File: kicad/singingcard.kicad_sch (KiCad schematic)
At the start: 0 parts

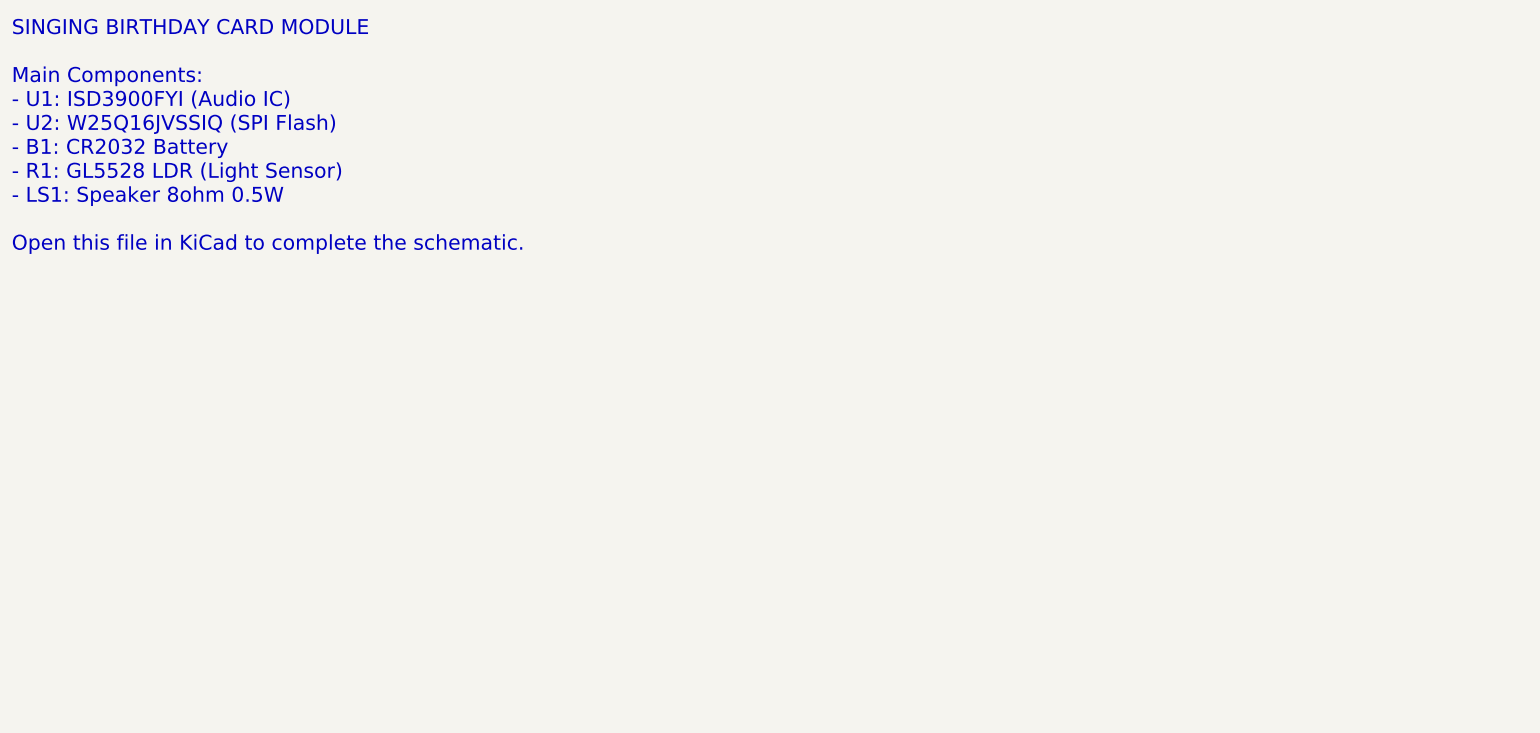
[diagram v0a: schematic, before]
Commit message: Add proper KiCad schematic with embedded symbols
- Created schematic generator scripts (v1-v5) to programmatically
  create KiCad schematics from SKiDL netlist data
- Final version (v5) places global labels at correct pin positions
- All 50 ERC violations are warnings (library config), not errors
- Updated kicad-agent.md skill with V-Model workflow approach
- Added render images for visual inspection
- Added DRC and ERC report files

🤖 Generated with [Claude Code](https://claude.com/claude-code)

Co-Authored-By: Claude <noreply@anthropic.com>
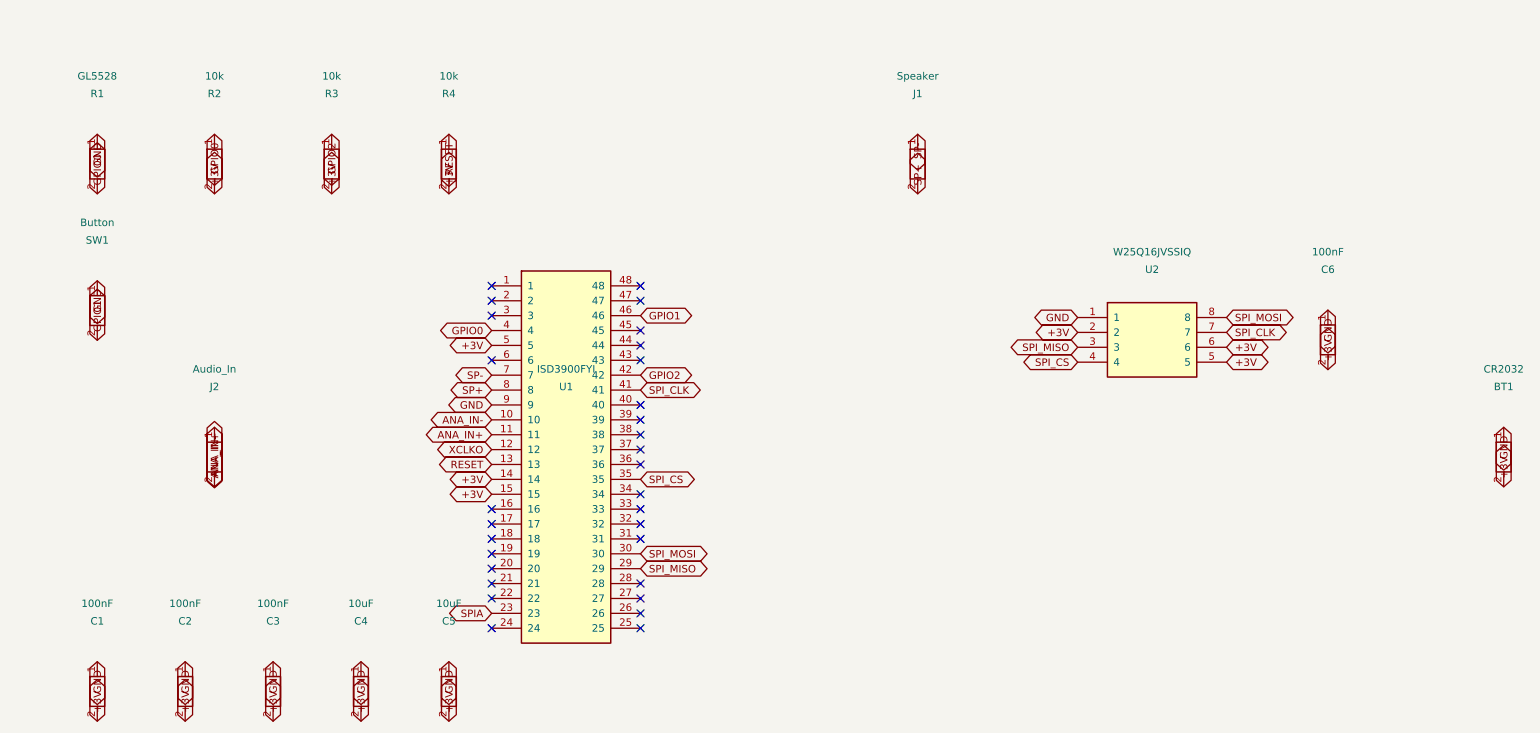
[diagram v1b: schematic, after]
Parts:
- added BT1: CR2032, singingcard:BAT-TH_CR2032-BS-6-1, symbol singingcard:CR2032
- added C1, C2, C3, C6: 100nF, Capacitor_SMD:C_0603_1608Metric, symbol singingcard:C
- added C4, C5: 10uF, Capacitor_SMD:C_0805_2012Metric, symbol singingcard:C
- added J1: Speaker, Connector_PinHeader_2.54mm:PinHeader_1x02_P2.54mm_Vertical, symbol singingcard:Conn_01x02
- added J2: Audio_In, Connector_PinHeader_2.54mm:PinHeader_1x02_P2.54mm_Vertical, symbol singingcard:Conn_01x02
- added R1: GL5528, singingcard:LDR_GL5528, symbol singingcard:LDR
- added R2, R3, R4: 10k, Resistor_SMD:R_0603_1608Metric, symbol singingcard:R
- added SW1: Button, Button_Switch_SMD:SW_SPST_B3U-1000P, symbol singingcard:SW_Push
- added U1: ISD3900FYI, singingcard:LQFP-48_7x7mm_P0.5mm, symbol singingcard:ISD3900FYI
- added U2: W25Q16JVSSIQ, singingcard:SOIC-8_5.23x5.23mm_P1.27mm, symbol singingcard:W25Q16JVSSIQ
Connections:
- new net +3V: BT1.2, C1.2, C2.2, C3.2, C4.2, C5.2, C6.2, R2.2, R3.2, R4.2, U1.14, U1.15, U1.5, U2.2, U2.5, U2.6
- new net ANA_IN+: J2.2, U1.11
- new net ANA_IN-: J2.1, U1.10
- new net GND: BT1.1, C1.1, C2.1, C3.1, C4.1, C5.1, C6.1, R1.1, SW1.1, U1.9, U2.1
- new net GPIO0: R1.2, R2.1, U1.4
- new net GPIO1: SW1.2, U1.46
- new net GPIO2: R3.1, U1.42
- new net RESET: R4.1, U1.13
- new net SP+: J1.2, U1.8
- new net SP-: J1.1, U1.7
- new net SPIA: U1.23
- new net SPI_CLK: U1.41, U2.7
- new net SPI_CS: U1.35, U2.4
- new net SPI_MISO: U1.29, U2.3
- new net SPI_MOSI: U1.30, U2.8
- new net XCLKO: U1.12
- no-connect marks 0 -> 30
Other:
- note removed: "SINGING BIRTHDAY CARD MODULE Main Components: - U1: ISD3900FYI (Audio IC) - U2: W25Q16JVSSIQ (SPI Flash) - B1: CR2032 Battery - R1: GL5528 LDR (Light Sensor) - LS1: Speaker 8ohm 0.5W Open this file in KiCad to complete the schematic."

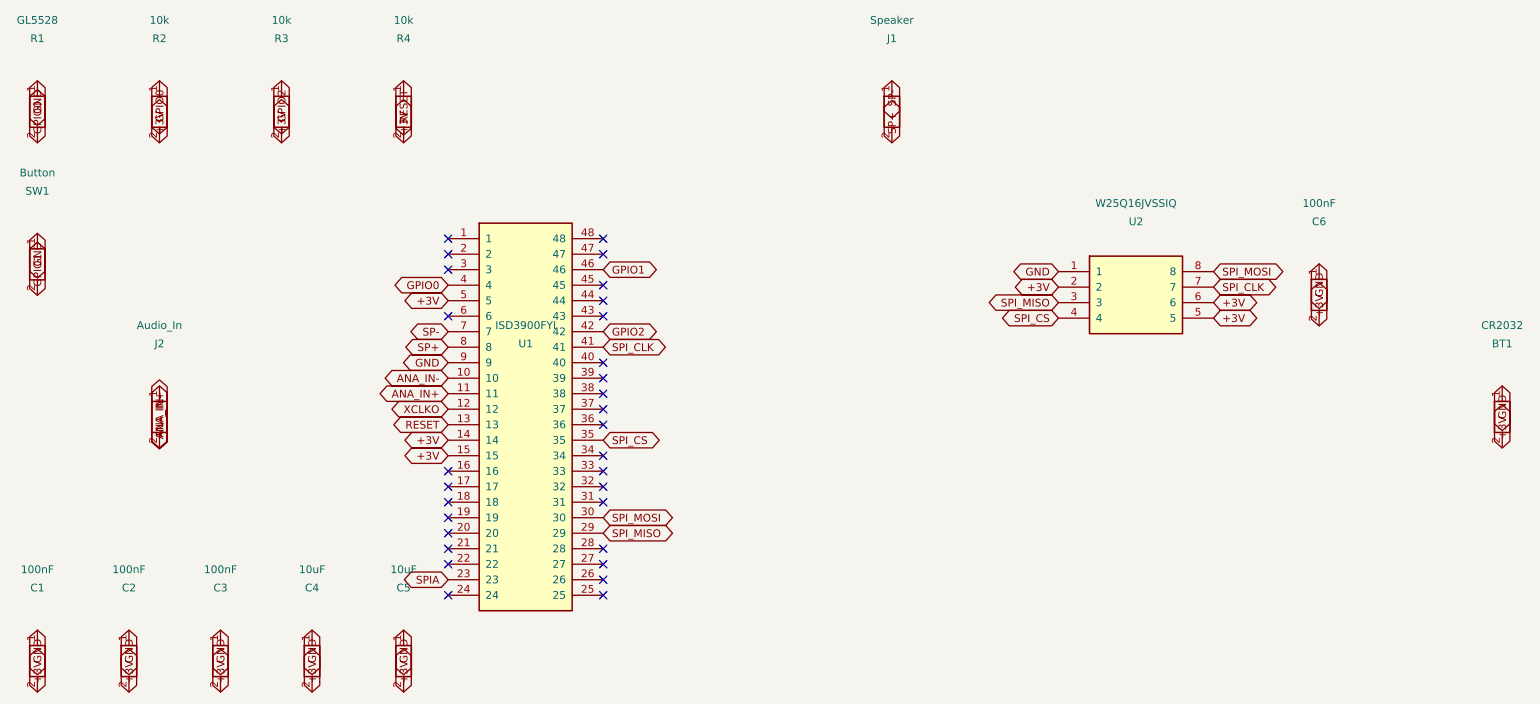
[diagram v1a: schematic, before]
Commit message: Complete schematic/ERC/DRC workflow and generate fab files
- Fixed schematic generator to use correct footprint names
- Created local symbol and footprint libraries
- ERC: 12 warnings (library config), 0 errors
- DRC: 26 warnings (cosmetic), 0 errors, 0 unconnected
- PCB fully routed with 188 tracks and vias
- Generated Gerber, drill, and position files for JLCPCB
- Created JLCPCB-ready zip file
- Updated skill file with ERC/DRC severity guidance
- Added final renders for visual inspection

🤖 Generated with [Claude Code](https://claude.com/claude-code)

Co-Authored-By: Claude <noreply@anthropic.com>
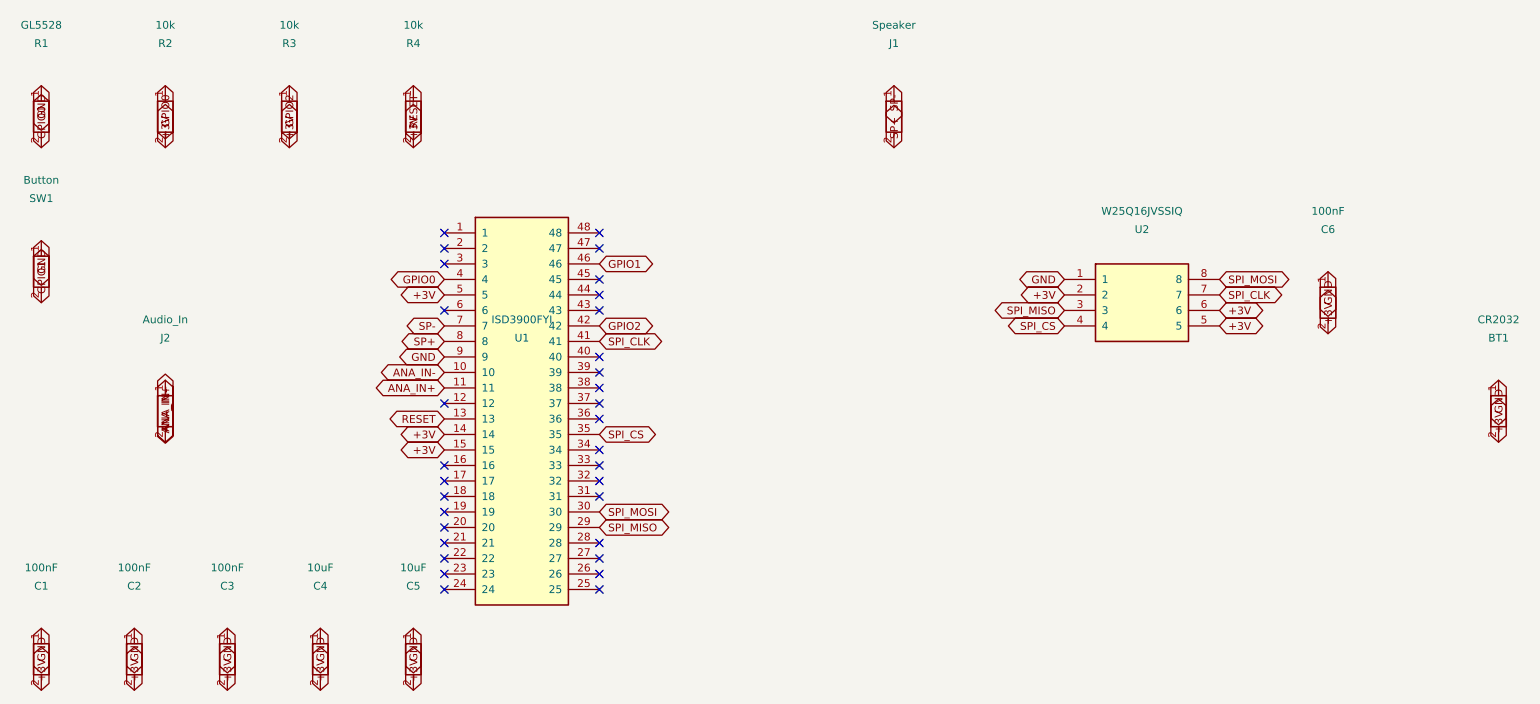
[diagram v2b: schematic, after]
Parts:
- R1: footprint singingcard:LDR_GL5528 -> singingcard:RES-TH_L5.1-W4.3-P3.40-D0.5
- SW1: footprint Button_Switch_SMD:SW_SPST_B3U-1000P -> Button_Switch_SMD:SW_SPST_TL3342
- U1: footprint singingcard:LQFP-48_7x7mm_P0.5mm -> singingcard:LQFP-48_L7.0-W7.0-P0.50-LS9.0-BL
- U2: footprint singingcard:SOIC-8_5.23x5.23mm_P1.27mm -> singingcard:SOIC-8_L5.3-W5.3-P1.27-LS8.0-BL
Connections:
- net SPIA: no longer names the net of U1.23
- net XCLKO: no longer names the net of U1.12
- no-connect marks 30 -> 32

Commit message: Add SMD speaker, fix component placement, clean up renders
- Replace J1 connector with LS1 SMD speaker (KLJ-01304T-08R07W, LCSC C18186315)
- Move U2 and C6 outside battery holder area to prevent overlap
- Move battery holder to meet 0.5mm edge clearance requirement
- Re-route PCB with FreeRouting (181 tracks, 21 vias)
- DRC passes with 0 errors, 0 unconnected items
- Change schematic page size from A3 to A4
- Clean up old render images, keep only current versions
- Update fabrication files (JLCPCB-ready zip)

🤖 Generated with [Claude Code](https://claude.com/claude-code)

Co-Authored-By: Claude <noreply@anthropic.com>
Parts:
- removed J1: Speaker, Connector_PinHeader_2.54mm:PinHeader_1x02_P2.54mm_Vertical, symbol singingcard:Conn_01x02
- added LS1: KLJ-01304T-08R07W, speaker:BUZ-SMD_4P-L13.0-W13.0-P11.4-BL, symbol singingcard:Speaker
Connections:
- net SP+: now also LS1.2
- net SP-: now also LS1.1
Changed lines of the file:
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@@
 	(generator "create_schematic_v5.py")
 	(generator_version "9.0")
-	(paper "A3")
+	(paper "A4")
 	(title_block
 		(title "Singing Birthday Card Module")
@@
 		(instances
 			(project "singingcard"
-				(path "/2e7227eb-1eb1-499c-8b75-1e8bc0de66c6"
+				(path "/eec44ccf-5c95-4f89-ae7a-d454166c2201"
 					(reference "U1")
 					(unit 1)
@@
 		(instances
 			(project "singingcard"
-				(path "/2e7227eb-1eb1-499c-8b75-1e8bc0de66c6"
+				(path "/eec44ccf-5c95-4f89-ae7a-d454166c2201"
 					(reference "U2")
 					(unit 1)
@@
 		(instances
 			(project "singingcard"
-				(path "/2e7227eb-1eb1-499c-8b75-1e8bc0de66c6"
+				(path "/eec44ccf-5c95-4f89-ae7a-d454166c2201"
 					(reference "BT1")
 					(unit 1)
@@
 		(instances
 			(project "singingcard"
-				(path "/2e7227eb-1eb1-499c-8b75-1e8bc0de66c6"
+				(path "/eec44ccf-5c95-4f89-ae7a-d454166c2201"
 					(reference "R1")
 					(unit 1)
@@
 		(instances
 			(project "singingcard"
-				(path "/2e7227eb-1eb1-499c-8b75-1e8bc0de66c6"
+				(path "/eec44ccf-5c95-4f89-ae7a-d454166c2201"
 					(reference "R2")
 					(unit 1)
@@
 		(instances
 			(project "singingcard"
-				(path "/2e7227eb-1eb1-499c-8b75-1e8bc0de66c6"
+				(path "/eec44ccf-5c95-4f89-ae7a-d454166c2201"
 					(reference "R3")
 					(unit 1)
@@
 		(instances
 			(project "singingcard"
-				(path "/2e7227eb-1eb1-499c-8b75-1e8bc0de66c6"
+				(path "/eec44ccf-5c95-4f89-ae7a-d454166c2201"
 					(reference "R4")
 					(unit 1)
@@
 		(instances
 			(project "singingcard"
-				(path "/2e7227eb-1eb1-499c-8b75-1e8bc0de66c6"
+				(path "/eec44ccf-5c95-4f89-ae7a-d454166c2201"
 					(reference "C1")
 					(unit 1)
@@
 		(instances
 			(project "singingcard"
-				(path "/2e7227eb-1eb1-499c-8b75-1e8bc0de66c6"
+				(path "/eec44ccf-5c95-4f89-ae7a-d454166c2201"
 					(reference "C2")
 					(unit 1)
@@
 		(instances
 			(project "singingcard"
-				(path "/2e7227eb-1eb1-499c-8b75-1e8bc0de66c6"
+				(path "/eec44ccf-5c95-4f89-ae7a-d454166c2201"
 					(reference "C3")
 					(unit 1)
@@
 		(instances
 			(project "singingcard"
-				(path "/2e7227eb-1eb1-499c-8b75-1e8bc0de66c6"
+				(path "/eec44ccf-5c95-4f89-ae7a-d454166c2201"
 					(reference "C4")
 					(unit 1)
@@
 		(instances
 			(project "singingcard"
-				(path "/2e7227eb-1eb1-499c-8b75-1e8bc0de66c6"
+				(path "/eec44ccf-5c95-4f89-ae7a-d454166c2201"
 					(reference "C5")
 					(unit 1)
@@
 		(instances
 			(project "singingcard"
-				(path "/2e7227eb-1eb1-499c-8b75-1e8bc0de66c6"
+				(path "/eec44ccf-5c95-4f89-ae7a-d454166c2201"
 					(reference "C6")
 					(unit 1)
@@
 	)
 	(symbol
-		(lib_id "singingcard:Conn_01x02")
+		(lib_id "singingcard:Speaker")
 		(at 180.34 50.8 0)
 		(unit 1)
@@
 		(on_board yes)
 		(dnp no)
-		(property "Reference" "J1"
+		(property "Reference" "LS1"
 			(at 180.34 38.8 0)
 			(effects
@@
 			)
 		)
-		(property "Value" "Speaker"
+		(property "Value" "KLJ-01304T-08R07W"
 			(at 180.34 35.8 0)
 			(effects
@@
 			)
 		)
-		(property "Footprint" "Connector_PinHeader_2.54mm:PinHeader_1x02_P2.54mm_Vertical"
+		(property "Footprint" "speaker:BUZ-SMD_4P-L13.0-W13.0-P11.4-BL"
 			(at 180.34 50.8 0)
 			(effects
@@
 			)
 		)
-		(property "Description" "Speaker connector"
+		(property "Description" "SMD Speaker 8ohm 700mW"
 			(at 180.34 50.8 0)
 			(effects
@@
 		(instances
 			(project "singingcard"
-				(path "/2e7227eb-1eb1-499c-8b75-1e8bc0de66c6"
-					(reference "J1")
+				(path "/eec44ccf-5c95-4f89-ae7a-d454166c2201"
+					(reference "LS1")
 					(unit 1)
 				)
@@
 		(instances
 			(project "singingcard"
-				(path "/2e7227eb-1eb1-499c-8b75-1e8bc0de66c6"
+				(path "/eec44ccf-5c95-4f89-ae7a-d454166c2201"
 					(reference "J2")
 					(unit 1)
@@
 		(instances
 			(project "singingcard"
-				(path "/2e7227eb-1eb1-499c-8b75-1e8bc0de66c6"
+				(path "/eec44ccf-5c95-4f89-ae7a-d454166c2201"
 					(reference "SW1")
 					(unit 1)
